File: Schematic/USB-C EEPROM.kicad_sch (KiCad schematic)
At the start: 6 parts, among them U9 CAT24C512WI-GT3

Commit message: added sensors?
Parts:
- added C71: 1u, symbol Device:C
- renumbered C52 to C70, R93 to R89, R92 to R90, R94 to R92, U9 to U8
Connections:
- net GND: now also C71.2
- net LDO_3V3: now also C71.1
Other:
- note added: "1010 ???? GND=0 so this: 1010 0000 -> 0x50 which is what we need for our PD controller"
- note added: "512Kb"
- note added: "Flash this with the bin taken from TI's website. Use I2C to USB adapter. Flash this when the system is off (not powered), only flash/power this."

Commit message: 1st Schematic Review
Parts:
- renumbered C70 to C73, C71 to C74, R89 to R91, R90 to R92, R91 to R93, R92 to R94, U8 to U11
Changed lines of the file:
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@@
 		(on_board yes)
 		(dnp no)
-		(property "Reference" "R91"
+		(property "Reference" "R93"
 			(at 115.316 101.854 0)
 			(effects
@@
 			(project "STAR"
 				(path "/fc8533bc-25dd-4c20-9b4c-ffebebd6739b/ec72a35b-e7f2-4422-8859-60e9fb848154/c75e3b3c-5e7c-48a1-b9c1-6d22fff06a0f"
-					(reference "R91")
+					(reference "R93")
 					(unit 1)
 				)
@@
 		(on_board yes)
 		(dnp no)
-		(property "Reference" "#PWR049"
+		(property "Reference" "#PWR054"
 			(at 107.95 119.38 0)
 			(effects
@@
 			(project "STAR"
 				(path "/fc8533bc-25dd-4c20-9b4c-ffebebd6739b/ec72a35b-e7f2-4422-8859-60e9fb848154/c75e3b3c-5e7c-48a1-b9c1-6d22fff06a0f"
-					(reference "#PWR049")
+					(reference "#PWR054")
 					(unit 1)
 				)
@@
 		(on_board yes)
 		(dnp no)
-		(property "Reference" "R90"
+		(property "Reference" "R92"
 			(at 110.236 101.854 0)
 			(effects
@@
 			(project "STAR"
 				(path "/fc8533bc-25dd-4c20-9b4c-ffebebd6739b/ec72a35b-e7f2-4422-8859-60e9fb848154/c75e3b3c-5e7c-48a1-b9c1-6d22fff06a0f"
-					(reference "R90")
+					(reference "R92")
 					(unit 1)
 				)
@@
 		(on_board yes)
 		(dnp no)
-		(property "Reference" "C70"
+		(property "Reference" "C73"
 			(at 193.04 102.108 0)
 			(effects
@@
 			(project "STAR"
 				(path "/fc8533bc-25dd-4c20-9b4c-ffebebd6739b/ec72a35b-e7f2-4422-8859-60e9fb848154/c75e3b3c-5e7c-48a1-b9c1-6d22fff06a0f"
-					(reference "C70")
+					(reference "C73")
 					(unit 1)
 				)
@@
 		(on_board yes)
 		(dnp no)
-		(property "Reference" "R92"
+		(property "Reference" "R94"
 			(at 186.436 100.584 0)
 			(effects
@@
 			(project "STAR"
 				(path "/fc8533bc-25dd-4c20-9b4c-ffebebd6739b/ec72a35b-e7f2-4422-8859-60e9fb848154/c75e3b3c-5e7c-48a1-b9c1-6d22fff06a0f"
-					(reference "R92")
+					(reference "R94")
 					(unit 1)
 				)
@@
 		(on_board yes)
 		(dnp no)
-		(property "Reference" "R89"
+		(property "Reference" "R91"
 			(at 105.156 101.854 0)
 			(effects
@@
 			(project "STAR"
 				(path "/fc8533bc-25dd-4c20-9b4c-ffebebd6739b/ec72a35b-e7f2-4422-8859-60e9fb848154/c75e3b3c-5e7c-48a1-b9c1-6d22fff06a0f"
-					(reference "R89")
+					(reference "R91")
 					(unit 1)
 				)
@@
 		(on_board yes)
 		(dnp no)
-		(property "Reference" "C71"
+		(property "Reference" "C74"
 			(at 199.39 102.108 0)
 			(effects
@@
 			(project "STAR"
 				(path "/fc8533bc-25dd-4c20-9b4c-ffebebd6739b/ec72a35b-e7f2-4422-8859-60e9fb848154/c75e3b3c-5e7c-48a1-b9c1-6d22fff06a0f"
-					(reference "C71")
+					(reference "C74")
 					(unit 1)
 				)
@@
 		(on_board yes)
 		(dnp no)
-		(property "Reference" "U8"
+		(property "Reference" "U11"
 			(at 157.48 88.9 0)
 			(effects
@@
 			(project ""
 				(path "/fc8533bc-25dd-4c20-9b4c-ffebebd6739b/ec72a35b-e7f2-4422-8859-60e9fb848154/c75e3b3c-5e7c-48a1-b9c1-6d22fff06a0f"
-					(reference "U8")
+					(reference "U11")
 					(unit 1)
 				)

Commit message: updates
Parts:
- renumbered R91 to R96, R92 to R97, R93 to R98, R94 to R99
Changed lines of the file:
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@@
 		(on_board yes)
 		(dnp no)
-		(property "Reference" "R93"
+		(property "Reference" "R98"
 			(at 115.316 101.854 0)
 			(effects
@@
 			(project "STAR"
 				(path "/fc8533bc-25dd-4c20-9b4c-ffebebd6739b/ec72a35b-e7f2-4422-8859-60e9fb848154/c75e3b3c-5e7c-48a1-b9c1-6d22fff06a0f"
-					(reference "R93")
+					(reference "R98")
 					(unit 1)
 				)
@@
 		(on_board yes)
 		(dnp no)
-		(property "Reference" "R92"
+		(property "Reference" "R97"
 			(at 110.236 101.854 0)
 			(effects
@@
 			(project "STAR"
 				(path "/fc8533bc-25dd-4c20-9b4c-ffebebd6739b/ec72a35b-e7f2-4422-8859-60e9fb848154/c75e3b3c-5e7c-48a1-b9c1-6d22fff06a0f"
-					(reference "R92")
+					(reference "R97")
 					(unit 1)
 				)
@@
 		(on_board yes)
 		(dnp no)
-		(property "Reference" "R94"
+		(property "Reference" "R99"
 			(at 186.436 100.584 0)
 			(effects
@@
 			(project "STAR"
 				(path "/fc8533bc-25dd-4c20-9b4c-ffebebd6739b/ec72a35b-e7f2-4422-8859-60e9fb848154/c75e3b3c-5e7c-48a1-b9c1-6d22fff06a0f"
-					(reference "R94")
+					(reference "R99")
 					(unit 1)
 				)
@@
 		(on_board yes)
 		(dnp no)
-		(property "Reference" "R91"
+		(property "Reference" "R96"
 			(at 105.156 101.854 0)
 			(effects
@@
 			(project "STAR"
 				(path "/fc8533bc-25dd-4c20-9b4c-ffebebd6739b/ec72a35b-e7f2-4422-8859-60e9fb848154/c75e3b3c-5e7c-48a1-b9c1-6d22fff06a0f"
-					(reference "R91")
+					(reference "R96")
 					(unit 1)
 				)

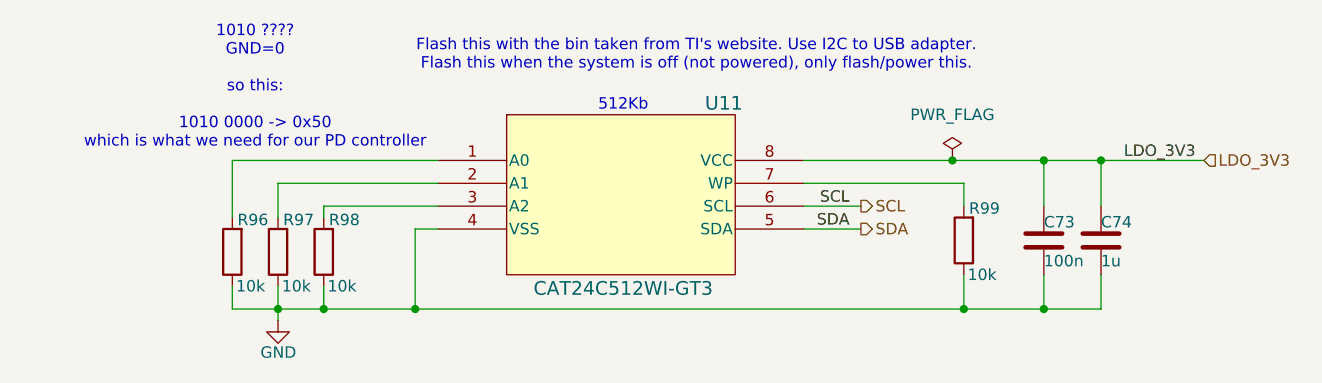
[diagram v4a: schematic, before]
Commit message: updated fuel guage
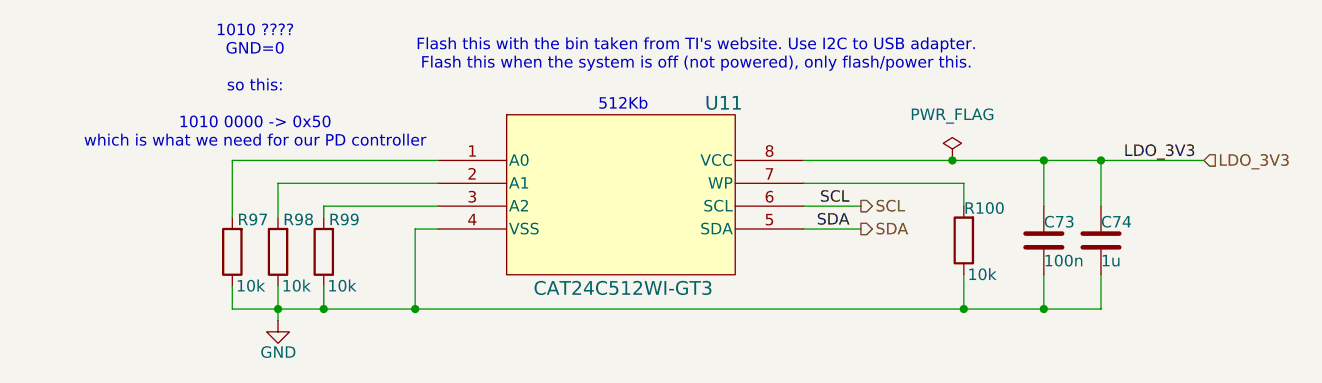
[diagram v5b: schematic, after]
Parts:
- renumbered R99 to R100, R96 to R97, R97 to R98, R98 to R99
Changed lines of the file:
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@@
 		(on_board yes)
 		(dnp no)
-		(property "Reference" "R98"
+		(property "Reference" "R99"
 			(at 115.316 101.854 0)
 			(effects
@@
 			(project "STAR"
 				(path "/fc8533bc-25dd-4c20-9b4c-ffebebd6739b/ec72a35b-e7f2-4422-8859-60e9fb848154/c75e3b3c-5e7c-48a1-b9c1-6d22fff06a0f"
-					(reference "R98")
+					(reference "R99")
 					(unit 1)
 				)
@@
 		(on_board yes)
 		(dnp no)
-		(property "Reference" "R97"
+		(property "Reference" "R98"
 			(at 110.236 101.854 0)
 			(effects
@@
 			(project "STAR"
 				(path "/fc8533bc-25dd-4c20-9b4c-ffebebd6739b/ec72a35b-e7f2-4422-8859-60e9fb848154/c75e3b3c-5e7c-48a1-b9c1-6d22fff06a0f"
-					(reference "R97")
+					(reference "R98")
 					(unit 1)
 				)
@@
 		(on_board yes)
 		(dnp no)
-		(property "Reference" "R99"
+		(property "Reference" "R100"
 			(at 186.436 100.584 0)
 			(effects
@@
 			(project "STAR"
 				(path "/fc8533bc-25dd-4c20-9b4c-ffebebd6739b/ec72a35b-e7f2-4422-8859-60e9fb848154/c75e3b3c-5e7c-48a1-b9c1-6d22fff06a0f"
-					(reference "R99")
+					(reference "R100")
 					(unit 1)
 				)
@@
 		(on_board yes)
 		(dnp no)
-		(property "Reference" "R96"
+		(property "Reference" "R97"
 			(at 105.156 101.854 0)
 			(effects
@@
 			(project "STAR"
 				(path "/fc8533bc-25dd-4c20-9b4c-ffebebd6739b/ec72a35b-e7f2-4422-8859-60e9fb848154/c75e3b3c-5e7c-48a1-b9c1-6d22fff06a0f"
-					(reference "R96")
+					(reference "R97")
 					(unit 1)
 				)

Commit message: Added MCU
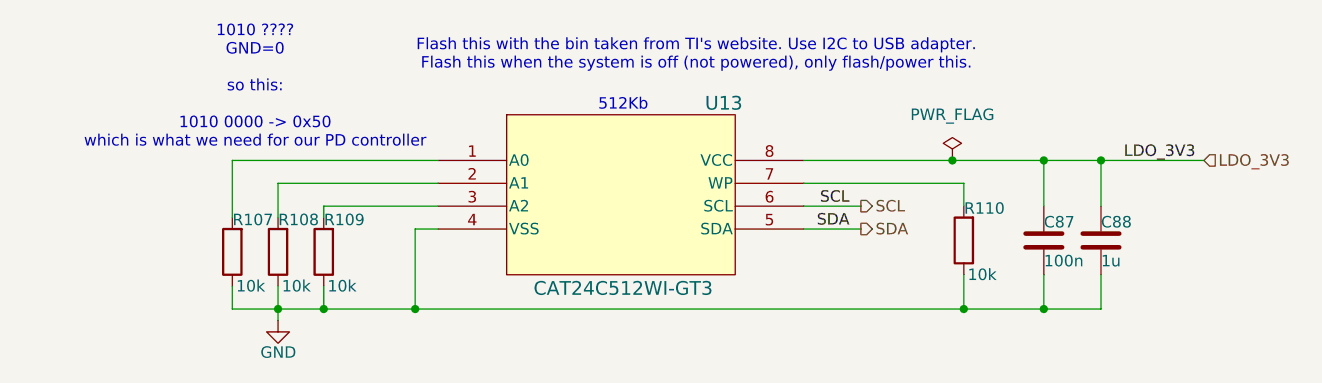
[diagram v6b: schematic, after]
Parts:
- renumbered C73 to C87, C74 to C88, R97 to R107, R98 to R108, R99 to R109, R100 to R110, U11 to U13
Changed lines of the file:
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@@
 		(on_board yes)
 		(dnp no)
-		(property "Reference" "R99"
+		(property "Reference" "R109"
 			(at 115.316 101.854 0)
 			(effects
@@
 			(project "STAR"
 				(path "/fc8533bc-25dd-4c20-9b4c-ffebebd6739b/ec72a35b-e7f2-4422-8859-60e9fb848154/c75e3b3c-5e7c-48a1-b9c1-6d22fff06a0f"
-					(reference "R99")
+					(reference "R109")
 					(unit 1)
 				)
@@
 		(on_board yes)
 		(dnp no)
-		(property "Reference" "#PWR055"
+		(property "Reference" "#PWR064"
 			(at 107.95 119.38 0)
 			(effects
@@
 			(project "STAR"
 				(path "/fc8533bc-25dd-4c20-9b4c-ffebebd6739b/ec72a35b-e7f2-4422-8859-60e9fb848154/c75e3b3c-5e7c-48a1-b9c1-6d22fff06a0f"
-					(reference "#PWR055")
+					(reference "#PWR064")
 					(unit 1)
 				)
@@
 		(on_board yes)
 		(dnp no)
-		(property "Reference" "R98"
+		(property "Reference" "R108"
 			(at 110.236 101.854 0)
 			(effects
@@
 			(project "STAR"
 				(path "/fc8533bc-25dd-4c20-9b4c-ffebebd6739b/ec72a35b-e7f2-4422-8859-60e9fb848154/c75e3b3c-5e7c-48a1-b9c1-6d22fff06a0f"
-					(reference "R98")
+					(reference "R108")
 					(unit 1)
 				)
@@
 		(on_board yes)
 		(dnp no)
-		(property "Reference" "C73"
+		(property "Reference" "C87"
 			(at 193.04 102.108 0)
 			(effects
@@
 			(project "STAR"
 				(path "/fc8533bc-25dd-4c20-9b4c-ffebebd6739b/ec72a35b-e7f2-4422-8859-60e9fb848154/c75e3b3c-5e7c-48a1-b9c1-6d22fff06a0f"
-					(reference "C73")
+					(reference "C87")
 					(unit 1)
 				)
@@
 		(on_board yes)
 		(dnp no)
-		(property "Reference" "R100"
+		(property "Reference" "R110"
 			(at 186.436 100.584 0)
 			(effects
@@
 			(project "STAR"
 				(path "/fc8533bc-25dd-4c20-9b4c-ffebebd6739b/ec72a35b-e7f2-4422-8859-60e9fb848154/c75e3b3c-5e7c-48a1-b9c1-6d22fff06a0f"
-					(reference "R100")
+					(reference "R110")
 					(unit 1)
 				)
@@
 		(on_board yes)
 		(dnp no)
-		(property "Reference" "R97"
+		(property "Reference" "R107"
 			(at 105.156 101.854 0)
 			(effects
@@
 			(project "STAR"
 				(path "/fc8533bc-25dd-4c20-9b4c-ffebebd6739b/ec72a35b-e7f2-4422-8859-60e9fb848154/c75e3b3c-5e7c-48a1-b9c1-6d22fff06a0f"
-					(reference "R97")
+					(reference "R107")
 					(unit 1)
 				)
@@
 		(on_board yes)
 		(dnp no)
-		(property "Reference" "C74"
+		(property "Reference" "C88"
 			(at 199.39 102.108 0)
 			(effects
@@
 			(project "STAR"
 				(path "/fc8533bc-25dd-4c20-9b4c-ffebebd6739b/ec72a35b-e7f2-4422-8859-60e9fb848154/c75e3b3c-5e7c-48a1-b9c1-6d22fff06a0f"
-					(reference "C74")
+					(reference "C88")
 					(unit 1)
 				)
@@
 		(on_board yes)
 		(dnp no)
-		(property "Reference" "U11"
+		(property "Reference" "U13"
 			(at 157.48 88.9 0)
 			(effects
@@
 			(project ""
 				(path "/fc8533bc-25dd-4c20-9b4c-ffebebd6739b/ec72a35b-e7f2-4422-8859-60e9fb848154/c75e3b3c-5e7c-48a1-b9c1-6d22fff06a0f"
-					(reference "U11")
+					(reference "U13")
 					(unit 1)
 				)

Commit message: Started to work on the BOM
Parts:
- C82: renamed from C87; footprint (none) -> Capacitor_SMD:C_1206_3216Metric_Pad1.33x1.80mm_HandSolder; Link (none) -> https://mou.sr/4n9ybmQ; Manufacturer Part Number (none) -> CL31B104KBCNNNC; Price per Unit (none) -> 0.11; Supplier (none) -> Mouser; Supplier Part Number (none) -> 187-CL31B104KBCNNNC
- C83: renamed from C88; footprint (none) -> Capacitor_SMD:C_1206_3216Metric_Pad1.33x1.80mm_HandSolder; Link (none) -> https://mou.sr/41y0aEA; Manufacturer Part Number (none) -> CL31B105KBHNNNE; Price per Unit (none) -> 0.11; Supplier (none) -> Mouser; Supplier Part Number (none) -> 187-CL31B105KBHNNNE
- U11: renamed from U13; footprint SOIC8_ONS -> (none)
- renumbered R107 to R103, R108 to R104, R109 to R105, R110 to R106

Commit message: Massive pivit, simplification
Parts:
- renumbered C82 to C75, C83 to C76, U11 to U10
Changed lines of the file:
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@@
+			)
+		)
+		(property "SNAPEDA_PACKAGE_ID" ""
+			(at 113.03 105.41 0)
+			(effects
+				(font
+					(size 1.27 1.27)
+				)
+				(hide yes)
 			)
 		)
@@
 		(on_board yes)
 		(dnp no)
-		(property "Reference" "#PWR059"
+		(property "Reference" "#PWR048"
 			(at 107.95 119.38 0)
 			(effects
@@
 			(project "STAR"
 				(path "/fc8533bc-25dd-4c20-9b4c-ffebebd6739b/ec72a35b-e7f2-4422-8859-60e9fb848154/c75e3b3c-5e7c-48a1-b9c1-6d22fff06a0f"
-					(reference "#PWR059")
+					(reference "#PWR048")
 					(unit 1)
 				)
@@
 			)
 		)
+		(property "SNAPEDA_PACKAGE_ID" ""
+			(at 107.95 105.41 0)
+			(effects
+				(font
+					(size 1.27 1.27)
+				)
+				(hide yes)
+			)
+		)
 		(pin "1"
 		)
@@
 		(on_board yes)
 		(dnp no)
-		(property "Reference" "C82"
+		(property "Reference" "C75"
 			(at 193.04 102.108 0)
 			(effects
@@
 		)
 		(property "Sim.Pins" ""
+			(at 193.04 104.14 0)
+			(effects
+				(font
+					(size 1.27 1.27)
+				)
+				(hide yes)
+			)
+		)
+		(property "SNAPEDA_PACKAGE_ID" ""
 			(at 193.04 104.14 0)
 			(effects
@@
 			(project "STAR"
 				(path "/fc8533bc-25dd-4c20-9b4c-ffebebd6739b/ec72a35b-e7f2-4422-8859-60e9fb848154/c75e3b3c-5e7c-48a1-b9c1-6d22fff06a0f"
-					(reference "C82")
+					(reference "C75")
 					(unit 1)
 				)
@@
 			)
 		)
+		(property "SNAPEDA_PACKAGE_ID" ""
+			(at 184.15 104.14 0)
+			(effects
+				(font
+					(size 1.27 1.27)
+				)
+				(hide yes)
+			)
+		)
 		(pin "1"
 		)
@@
 			)
 		)
+		(property "SNAPEDA_PACKAGE_ID" ""
+			(at 102.87 105.41 0)
+			(effects
+				(font
+					(size 1.27 1.27)
+				)
+				(hide yes)
+			)
+		)
 		(pin "1"
 		)
@@
 		(on_board yes)
 		(dnp no)
-		(property "Reference" "C83"
+		(property "Reference" "C76"
 			(at 199.39 102.108 0)
 			(effects
@@
 		)
 		(property "Sim.Pins" ""
+			(at 199.39 104.14 0)
+			(effects
+				(font
+					(size 1.27 1.27)
+				)
+				(hide yes)
+			)
+		)
+		(property "SNAPEDA_PACKAGE_ID" ""
 			(at 199.39 104.14 0)
 			(effects
@@
 			(project "STAR"
 				(path "/fc8533bc-25dd-4c20-9b4c-ffebebd6739b/ec72a35b-e7f2-4422-8859-60e9fb848154/c75e3b3c-5e7c-48a1-b9c1-6d22fff06a0f"
-					(reference "C83")
+					(reference "C76")
 					(unit 1)
 				)
@@
 		(on_board yes)
 		(dnp no)
-		(property "Reference" "U11"
+		(property "Reference" "U10"
 			(at 157.48 88.9 0)
 			(effects
@@
 		)
 		(property "Sim.Pins" ""
+			(at 125.73 95.25 0)
+			(effects
+				(font
+					(size 1.27 1.27)
+				)
+				(hide yes)
+			)
+		)
+		(property "SNAPEDA_PACKAGE_ID" ""
 			(at 125.73 95.25 0)
 			(effects
@@
 			(project ""
 				(path "/fc8533bc-25dd-4c20-9b4c-ffebebd6739b/ec72a35b-e7f2-4422-8859-60e9fb848154/c75e3b3c-5e7c-48a1-b9c1-6d22fff06a0f"
-					(reference "U11")
+					(reference "U10")
 					(unit 1)
 				)
